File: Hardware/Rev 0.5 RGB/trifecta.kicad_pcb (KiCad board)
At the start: 2 copper layers, 361 x 120.8 mm, 286 parts, among them J1 USB2_C_Receptacle, J2 ISP Header, SW1 RESET, SW2 Rotary_Encoder_Switch, SW3 Rotary_Encoder_Switch, SW4 Rotary_Encoder_Switch, U1 ATmega32U4-AU, U2 SRV05-4, Y1 16MHz

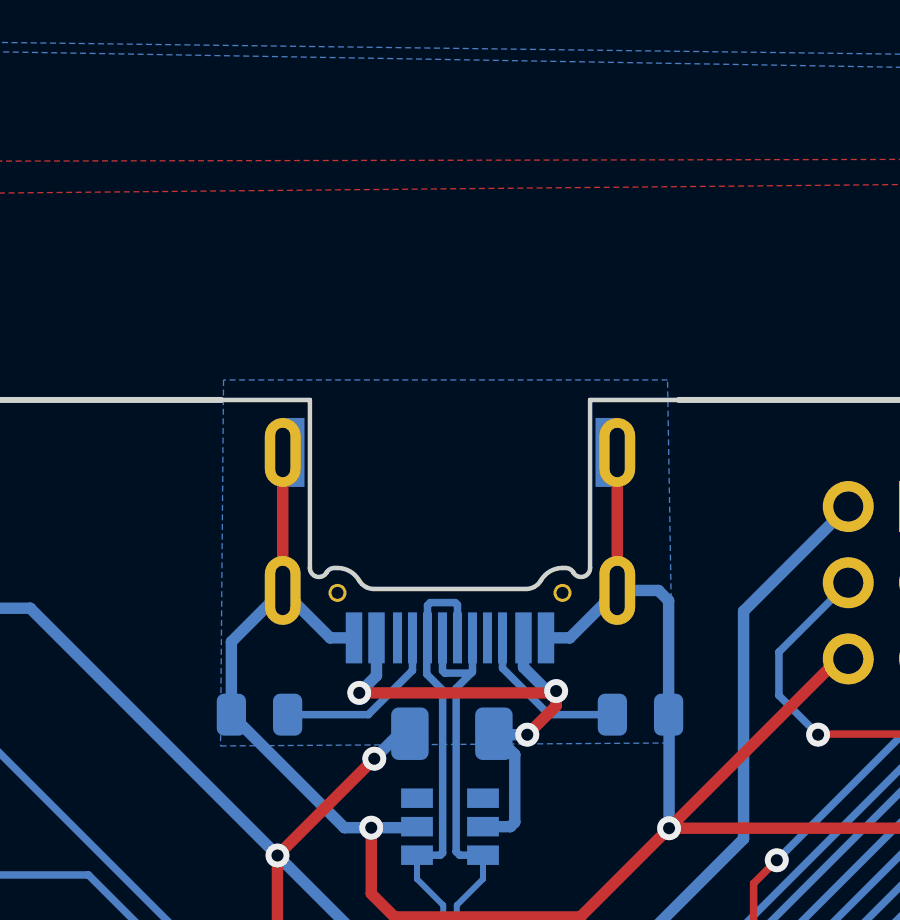
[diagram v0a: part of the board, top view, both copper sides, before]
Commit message: move usb port out
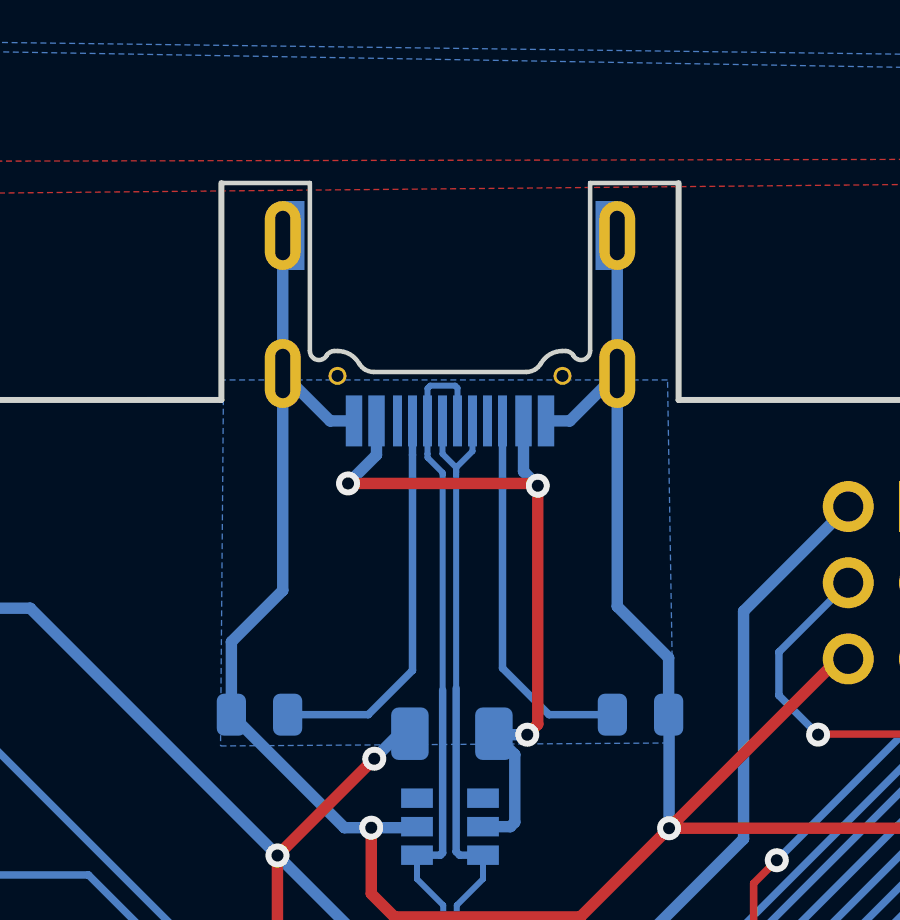
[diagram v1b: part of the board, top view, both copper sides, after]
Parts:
- moved J1 7.23 mm to (141.6, -12.8)
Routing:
- net GND: track 2438.5 -> 2452.3 mm
- net Net-(J1-PadA5): track 5.86 -> 13.1 mm
- net Net-(J1-PadB5): track 5.31 -> 12.5 mm
- net D-: track 45.4 -> 52.7 mm
- net D+: track 43.7 -> 50.7 mm
- net VBUS: track 18.4 -> 25.1 mm
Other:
- board size 361 x 120.8 mm -> 361 x 128 mm
